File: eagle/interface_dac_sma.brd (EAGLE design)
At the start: 109.5 x 126 mm, 28 parts, among them X1 BU-SMA-V

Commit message: code
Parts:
- U$2: value MCP4728DIL4 -> MCP4728DIL; device microchip:DIL10-04 -> microchip:DIL10
- moved R11 0.28 mm to (65.2, 86.6)
- moved R13 0.18 mm to (98.2, 87.1)
- moved R9 0.13 mm to (33.5, 86.5)
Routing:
- net GND: track 0.00 -> 83.3 mm
- net N$17: track 10.7 -> 13.3 mm
- net +12V: track 136.5 -> 139.1 mm
- net VCC: track 157.8 -> 160.3 mm
- net N$18: track 38.4 -> 40.6 mm
- net N$8: track 28.3 -> 29.7 mm
- net SDA_OUT: track 21.5 -> 22.7 mm
- net SCL_OUT: track 20.4 -> 21.7 mm
- net N$1: track 17.3 -> 18.3 mm
- net N$15: track 58.9 -> 59.4 mm
- net N$11: track 29.5 -> 30.0 mm
- net N$14: track 26.0 -> 25.5 mm

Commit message: add iso1540
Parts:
- removed R4, R5: 1k, rcl:0207/12
- added IC1: ISO1540, texas:DIL08
- R1, R2: value 100 -> 1.5k; device rcl:0207/12 -> resistor:0207/12
- moved R2 27.1 mm to (43.3, 58.7), turned to 180 degrees
- moved R1 24.6 mm to (56.6, 50.4), turned to 180 degrees
- moved OK1 13.5 mm to (26.7, 43.2)
- moved R3 8.90 mm to (23.7, 25.4)
- moved R18 8.90 mm to (18.5, 32.4)
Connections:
- removed net N$4: OK1.8, R1.1
- removed net N$5: OK1.6, R2.1
- net A+5: now also IC1.1
- net AGND: now also IC1.4; no longer R1.2, R2.2
- net GND: now also IC1.5; no longer R4.2, R5.2
- net SCL: now also IC1.3; no longer OK1.5
- net SCL_OUT: now also IC1.6, R2.1; no longer OK1.11, R5.1
- net SDA: now also IC1.2; no longer OK1.7
- net SDA_OUT: now also IC1.7, R1.1; no longer OK1.9, R4.1
- net VCC: now also IC1.8, R1.2, R2.2; no longer OK1.10, OK1.12
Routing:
- net AGND: track 210.9 -> 0.00 mm
- net VCC: track 160.3 -> 56.0 mm
- net ENSW1: track 39.0 -> 0.00 mm
- net ENSW2: track 26.1 -> 0.00 mm
- net SCL: track 23.5 -> 0.00 mm
- net PWM9: track 23.5 -> 0.00 mm
- net SDA_OUT: track 22.7 -> 0.00 mm
- net SDA: track 22.4 -> 0.00 mm
- net PWM6: track 22.4 -> 0.00 mm
- net SCL_OUT: track 21.7 -> 0.00 mm
- net N$10: track 14.7 -> 0.00 mm
- net N$4: track 14.6 -> 0.00 mm
- net N$5: track 7.93 -> 0.00 mm
- net N$7: track 7.62 -> 0.00 mm

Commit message: board tweak
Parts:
- moved IC1 22.8 mm to (61.6, 45.6), turned to 0 degrees
- moved R1 15.8 mm to (43.7, 59.4)
- moved CONTROLGD1 15.4 mm to (20.6, 74.7)
- moved CONTROLGD2 14.3 mm to (15.5, 61.8)
- moved R3 13.0 mm to (31.4, 35.9), turned to 0 degrees
- moved R2 8.64 mm to (43.7, 67.3)
- moved R18 6.17 mm to (13.6, 36.1)
- moved R9 4.70 mm to (33.7, 91.2)
- moved PCB1 4.70 mm to (17.3, 6.22)
- moved C4 4.70 mm to (98.3, 62.4)
- moved CONTROLHV 4.70 mm to (34.2, 118.6)
- moved POWERINTERFACE 4.70 mm to (92.0, 119.6)
- moved R10 4.70 mm to (49.8, 104.9)
- moved R11 4.70 mm to (65.3, 91.3)
- moved R12 4.70 mm to (81.7, 108.0)
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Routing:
- net VCC: track 56.0 -> 158.3 mm, vias 0 -> 2
- net AGND: track 0.00 -> 63.8 mm
- net A+5: track 0.00 -> 51.8 mm
- net SCL_OUT: track 0.00 -> 46.8 mm, vias 0 -> 2
- net SDA_OUT: track 0.00 -> 36.5 mm
- net SDA: track 0.00 -> 34.0 mm
- net SCL: track 0.00 -> 31.0 mm, vias 0 -> 2
- net PWM6: track 0.00 -> 27.8 mm
- net PWM9: track 0.00 -> 26.5 mm
- net ENSW1: track 0.00 -> 25.4 mm
- net ENSW2: track 0.00 -> 12.6 mm
- net N$10: track 0.00 -> 5.71 mm
- net N$7: track 0.00 -> 5.59 mm
- net N$12: track 9.20 -> 12.4 mm
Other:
- board size 109.5 x 126 mm -> 109.5 x 130.7 mm

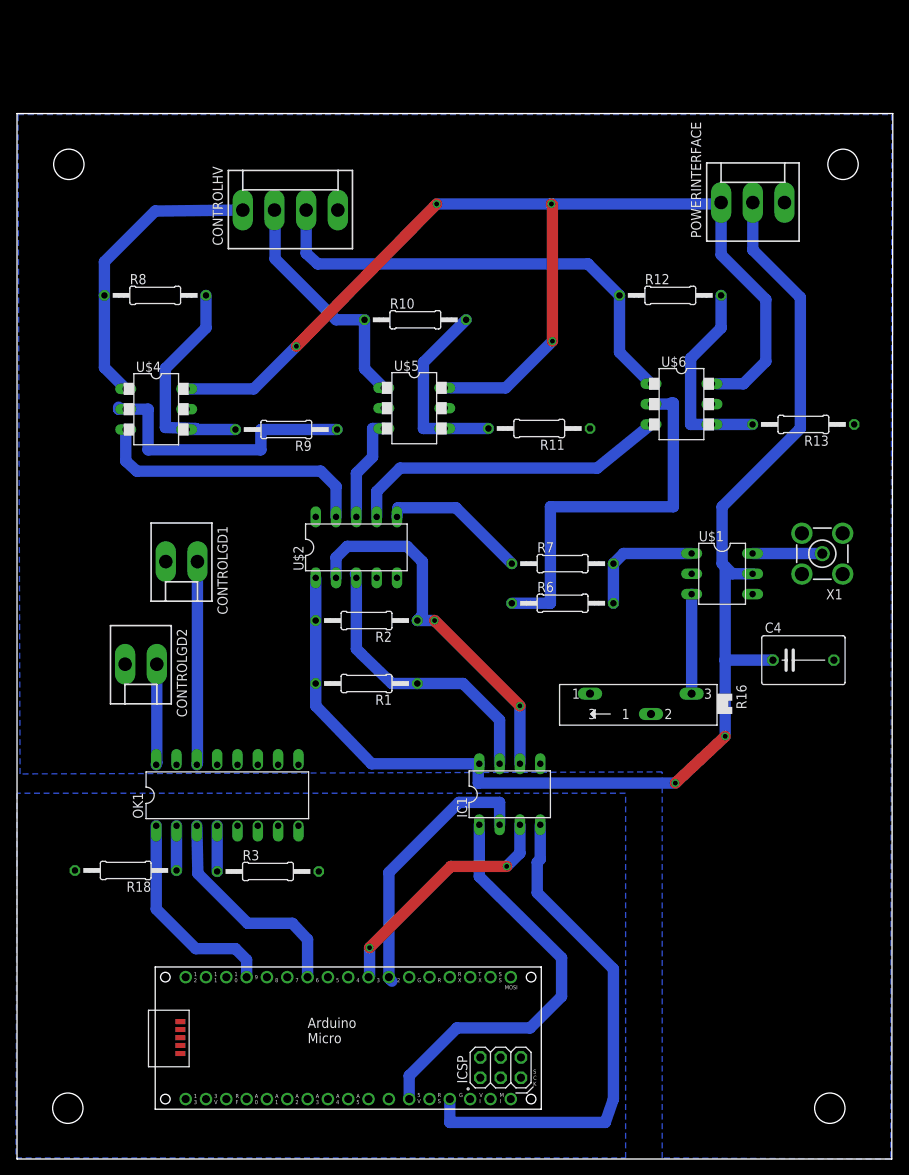
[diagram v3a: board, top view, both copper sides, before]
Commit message: Code debug, add darlingtons to HV input
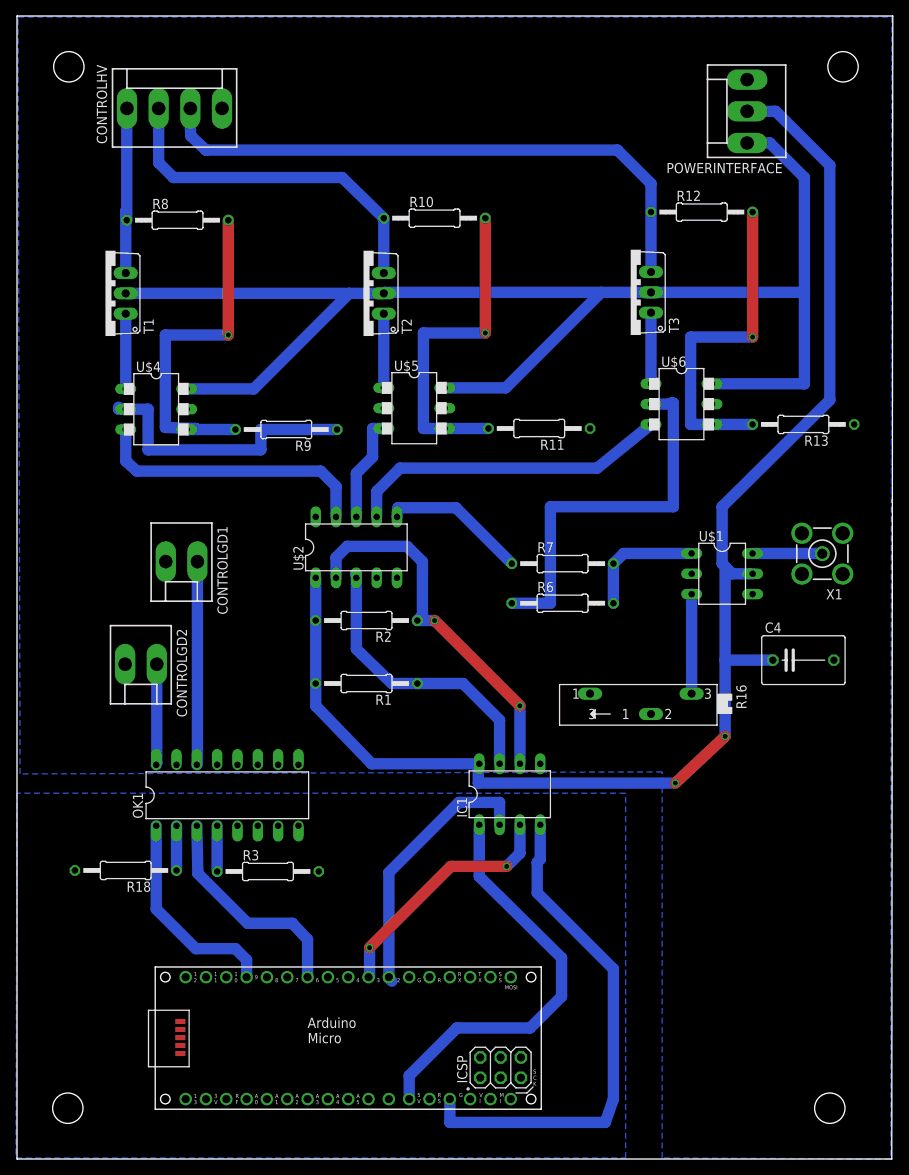
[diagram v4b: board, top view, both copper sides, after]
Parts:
- added T1, T2, T3: TIP122V, transistor-npn:TO220V
- moved CONTROLHV 19.3 mm to (19.7, 131.3)
- moved R10 12.9 mm to (52.2, 117.6)
- moved POWERINTERFACE 11.4 mm to (91.3, 131.0), turned to 90 degrees
- moved R12 11.1 mm to (85.6, 118.4)
- moved R8 9.80 mm to (20.1, 117.3)
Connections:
- new net N$4: CONTROLHV.1, R8.1, T1.3
- new net N$5: T1.1, U$4.1
- new net N$6: CONTROLHV.2, R10.1, T2.3
- net +12V: now also T1.2, T2.2, T3.2
- net N$11: now also CONTROLHV.3, R12.1, T3.3; no longer CONTROLHV.2, R10.1, U$5.1
- net N$15: now also T3.1; no longer CONTROLHV.3, R12.1
- net N$3: now also T2.1, U$5.1; no longer CONTROLHV.1, R8.1, U$4.1
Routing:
- net N$15: track 59.4 -> 8.89 mm
- net N$6: track 0.00 -> 44.6 mm
- net N$11: track 30.0 -> 74.5 mm
- net +12V: track 139.1 -> 181.1 mm, vias 4 -> 0
- net N$3: track 36.9 -> 9.27 mm
- net N$4: track 0.00 -> 22.9 mm
- net N$9: track 23.9 -> 42.2 mm, vias 0 -> 1
- net VCC: track 158.3 -> 175.2 mm
- net N$14: track 25.5 -> 42.0 mm, vias 0 -> 1
- net N$8: track 29.7 -> 44.8 mm, vias 0 -> 1
- net N$5: track 0.00 -> 9.40 mm
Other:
- board size 109.5 x 130.7 mm -> 109.5 x 142.9 mm

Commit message: darlington gate resistor, diode stacking
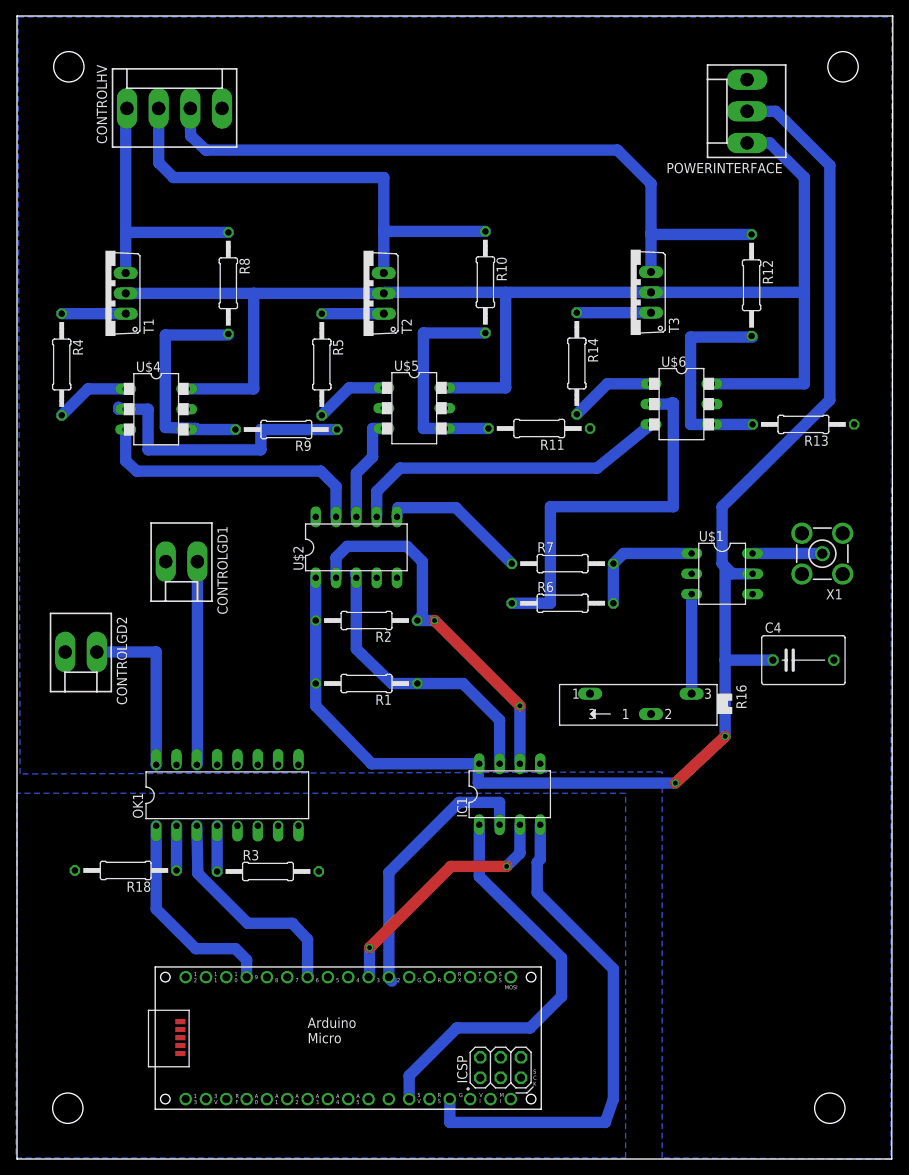
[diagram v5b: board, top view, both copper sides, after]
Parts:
- added R14, R4, R5: 14k, resistor:0207/12
- moved R12 11.1 mm to (91.8, 109.2), turned to 270 degrees
- moved R10 10.2 mm to (58.5, 109.6), turned to 270 degrees
- moved R8 10.1 mm to (26.4, 109.5), turned to 270 degrees
- moved CONTROLGD2 7.65 mm to (8.00, 63.4)
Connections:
- new net N$19: R4.2, U$4.1
- new net N$20: R5.2, U$5.1
- new net N$21: R14.2, U$6.1
- net N$15: now also R14.1; no longer U$6.1
- net N$3: now also R4.1, T1.1; no longer T2.1, U$5.1
- net N$5: now also R5.1, T2.1; no longer T1.1, U$4.1
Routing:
- net N$6: track 44.6 -> 60.3 mm
- net N$14: track 42.0 -> 26.4 mm, vias 1 -> 0
- net N$9: track 42.2 -> 27.8 mm, vias 1 -> 0
- net N$8: track 44.8 -> 30.5 mm, vias 1 -> 0
- net N$11: track 74.5 -> 87.0 mm
- net N$21: track 0.00 -> 10.8 mm
- net N$4: track 22.9 -> 33.5 mm
- net +12V: track 181.1 -> 171.2 mm
- net N$19: track 0.00 -> 9.37 mm
- net ENSW2: track 12.6 -> 21.8 mm
- net N$20: track 0.00 -> 9.17 mm
- net N$5: track 9.40 -> 7.75 mm
- net N$3: track 9.27 -> 8.00 mm
